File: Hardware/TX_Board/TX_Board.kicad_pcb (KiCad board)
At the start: 4 copper layers, 148 x 98.8 mm, 224 parts, among them IC1 GP2Y1+, IC10 QPA9122TR7, IC11 MAPS-010164-TR0500, IC12 QPA9122TR7, IC13 MAPS-010164-TR0500, IC14 QPA9122TR7, IC2 GP2Y1+, IC3 GP2Y1+, IC4 LT3041ADE#PBF, IC5 LT3099ADE#PBF, IC6 ADPL40502AUJZ-1.5-R7, IC7 MAPS-010164-TR0500, IC8 QPA9122TR7, IC9 MAPS-010164-TR0500, J1 Conn_Coaxial, J10 MM8030-2610RJ3, J11 MM8030-2610RJ3, J12 MM8030-2610RJ3, J13 MM8030-2610RJ3, J14 MM8030-2610RJ3, J15 Conn_Coaxial, J16 MM8030-2610RJ3, J17 MM8030-2610RJ3, J18 Conn_Coaxial, J19 MM8030-2610RJ3, J2 Conn_01x01_Pin, J20 MM8030-2610RJ3, J21 Conn_Coaxial, J22 MM8030-2610RJ3, J23 MM8030-2610RJ3, J24 Conn_Coaxial, J3 Conn_01x01_Pin, J4 Conn_01x01_Pin, J5 Conn_01x01_Pin, J6 Conn_02x12_Odd_Even, J7 Conn_01x03_Socket, J8 Conn_02x08_Odd_Even, J9 MM8030-2610RJ3, U1 SN74HCT138NSR

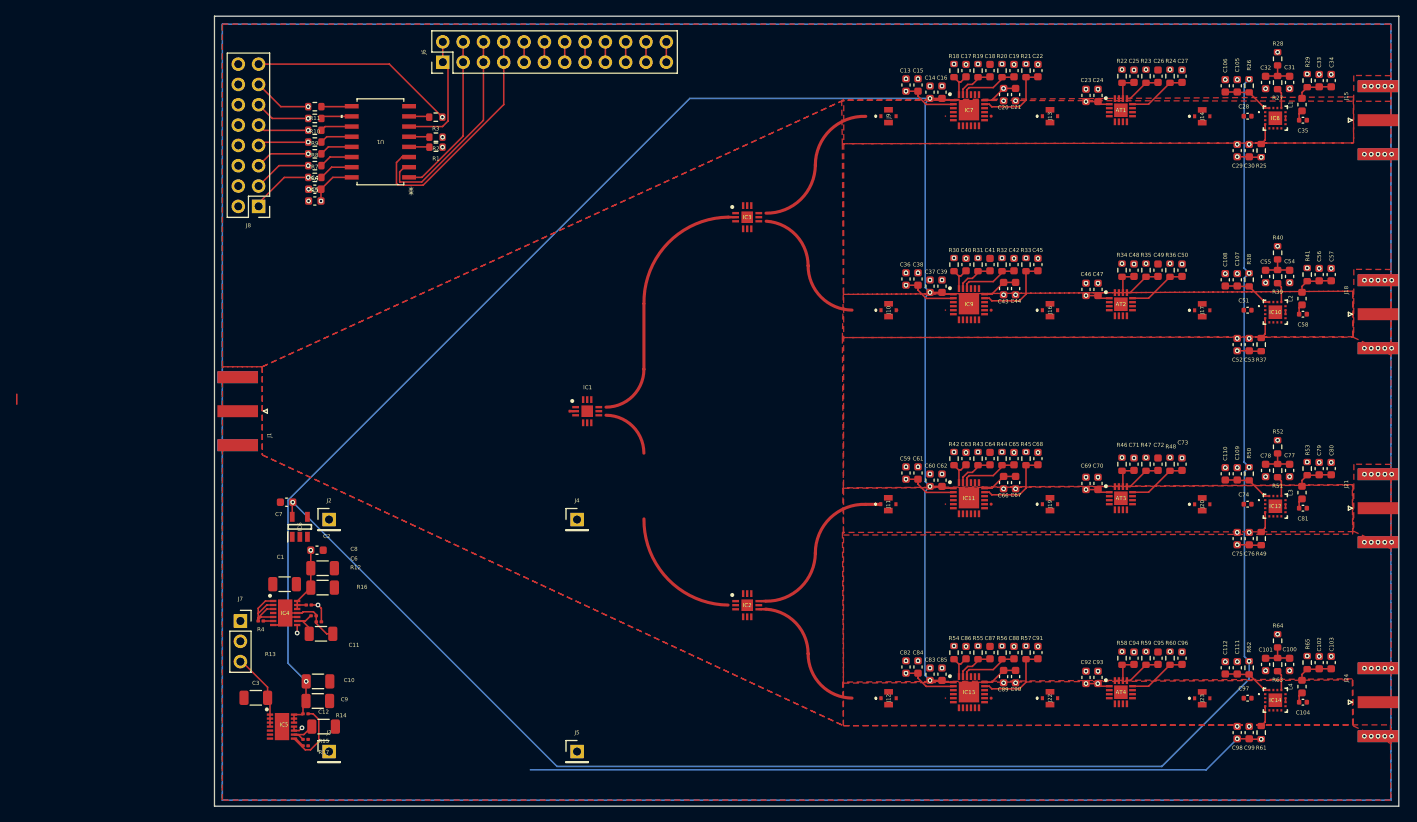
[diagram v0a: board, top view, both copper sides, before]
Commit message: Swapped layers
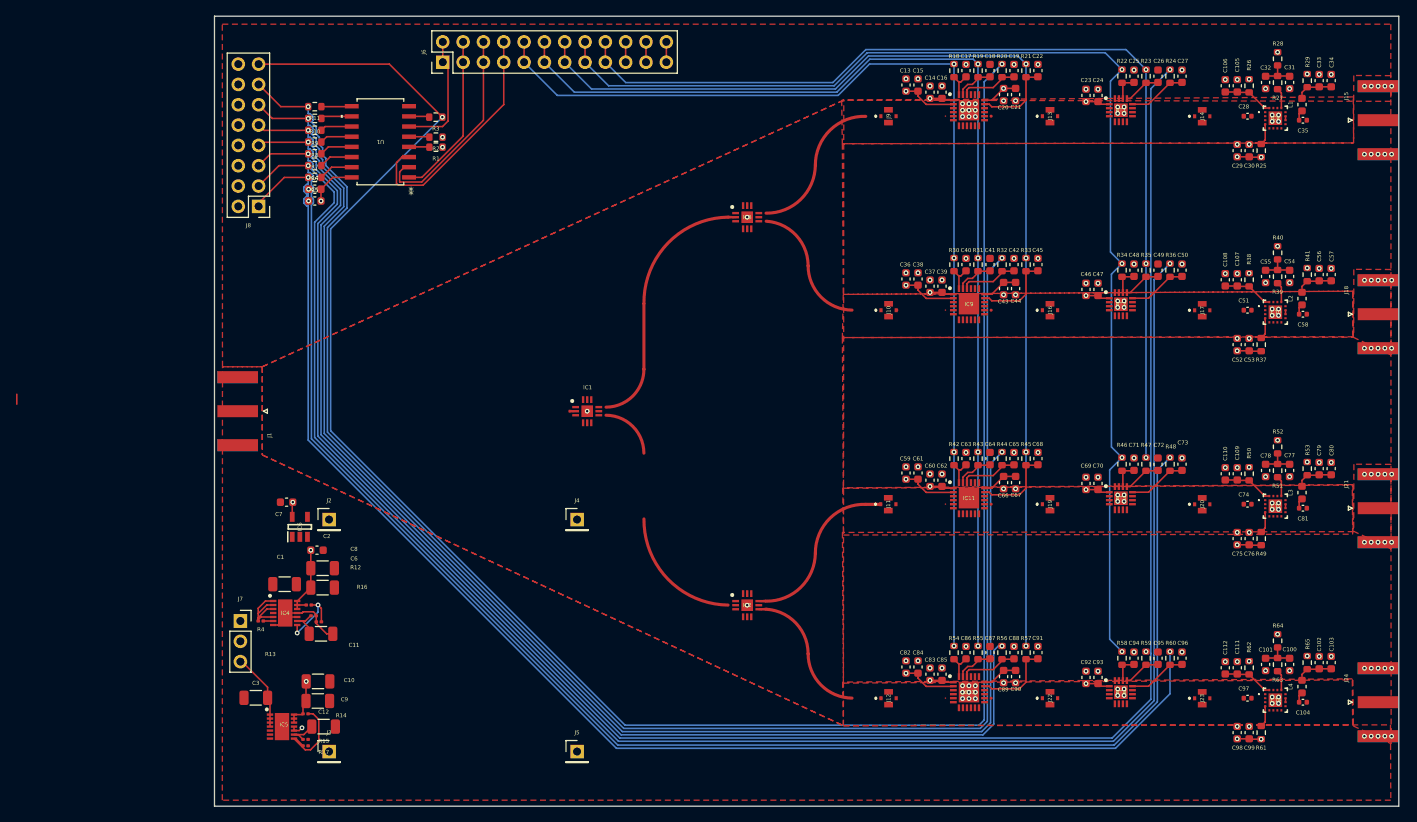
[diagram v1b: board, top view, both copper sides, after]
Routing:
- net PS_LE_3: track 177.7 -> 183.1 mm
- net PS_LE_2: track 202.9 -> 208.3 mm
- net PS_LE_1: track 245.5 -> 250.8 mm
- net PS_LE_4: track 154.6 -> 158.2 mm
- net ATTN_SI: track 146.2 -> 149.8 mm
- net ATTN_LE_2: track 219.8 -> 223.2 mm
- net ATTN_LE_1: track 244.1 -> 247.4 mm
- net ATTN_LE_3: track 194.2 -> 197.3 mm
- net VCC: vias 26 -> 25
- net GND: vias 129 -> 182
- added copper zone on In2.Cu, net VCC
- removed copper zone on B.Cu, net VCC

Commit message: Layout Tweaks
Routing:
- net VCC: track 175.2 -> 180.4 mm
- net VEE: track 217.3 -> 219.8 mm
- net GND: track 13.7 -> 11.8 mm, vias 182 -> 191
- net -VDC: track 9.57 -> 11.1 mm
- net Net-(IC5-PGFB): track 9.99 -> 11.3 mm
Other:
- board text added: "Phased and Confused Rev. 1 Rice ECE Capstone Team BEAMFORM"
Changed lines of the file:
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@@
 		(layer "Edge.Cuts")
 	)
+	(gr_text "Phased and Confused\nRev. 1\nRice ECE Capstone\nTeam BEAMFORM"
+		(at 84.529 68.072 0)
+		(layer "F.SilkS")
+		(effects
+			(font
+				(size 1.5 1.5)
+				(thickness 0.2)
+			)
+			(justify left bottom)
+		)
+	)
 	(gr_text "${REFERENCE}"
 		(at 183.195 49.88 270)
@@
 	)
 	(segment
-		(start 89.952 106.1)
-		(end 90.8 105.252)
+		(start 93.665 121.2)
+		(end 93.885 121.2)
 		(width 0.2)
 		(layer "F.Cu")
@@
 	)
 	(segment
-		(start 92.3 105.1)
-		(end 91.3 105.1)
+		(start 93.665 120.4)
+		(end 93.835 120.4)
 		(width 0.2)
 		(layer "F.Cu")
@@
 	)
 	(segment
-		(start 94.68 105.899999)
-		(end 95.980001 107.2)
+		(start 176.02 41.5)
+		(end 176.27 41.75)
+		(width 0.2)
+		(layer "F.Cu")
+		(net 1)
+	)
+	(segment
+		(start 92.3 105.1)
+		(end 91.3 105.1)
 		(width 0.2)
 		(layer "F.Cu")
@@
 	)
 	(segment
-		(start 91.3 105.1)
-		(end 90.8 104.6)
+		(start 94.68 105.899999)
+		(end 95.980001 107.2)
 		(width 0.2)
 		(layer "F.Cu")
@@
 	)
 	(segment
-		(start 94.67 104.79013)
-		(end 94.32887 104.449)
+		(start 93.885 121.2)
+		(end 94.26 120.825)
 		(width 0.2)
 		(layer "F.Cu")
@@
 	)
 	(segment
-		(start 92.3 104.6)
-		(end 90.8 104.6)
+		(start 94.67 104.79013)
+		(end 94.32887 104.449)
 		(width 0.2)
 		(layer "F.Cu")
@@
 	)
 	(segment
-		(start 90.8 105.252)
-		(end 90.8 104.6)
+		(start 94.32887 104.449)
+		(end 93.051 104.449)
 		(width 0.2)
 		(layer "F.Cu")
@@
 	)
 	(segment
-		(start 94.32887 104.449)
-		(end 93.051 104.449)
+		(start 93.835 120.4)
+		(end 94.26 120.825)
 		(width 0.2)
 		(layer "F.Cu")
@@
 	)
 	(segment
+		(start 176.02 42)
+		(end 176.27 41.75)
+		(width 0.2)
+		(layer "F.Cu")
+		(net 1)
+	)
+	(segment
 		(start 89.3 106.1)
 		(end 89.952 106.1)
@@
 	)
 	(via
+		(at 94.26 120.825)
+		(size 0.6)
+		(drill 0.3)
+		(layers "F.Cu" "B.Cu")
+		(free yes)
+		(net 1)
+	)
+	(via
 		(at 176.27 115.3)
 		(size 0.6)
@@
 	)
 	(via
+		(at 90.4 104.2)
+		(size 0.6)
+		(drill 0.3)
+		(layers "F.Cu" "B.Cu")
+		(net 1)
+	)
+	(via
 		(at 182.1 64.825)
 		(size 0.6)
@@
 	)
 	(via
+		(at 90.4 103.4)
+		(size 0.6)
+		(drill 0.3)
+		(layers "F.Cu" "B.Cu")
+		(net 1)
+	)
+	(via
 		(at 148.55 55.125)
 		(size 0.6)
@@
 	)
 	(via
+		(at 91.2 105.8)
+		(size 0.6)
+		(drill 0.3)
+		(layers "F.Cu" "B.Cu")
+		(net 1)
+	)
+	(via
 		(at 220.05 110.025)
 		(size 0.6)
@@
 	)
 	(via
+		(at 90.4 105)
+		(size 0.6)
+		(drill 0.3)
+		(layers "F.Cu" "B.Cu")
+		(net 1)
+	)
+	(via
 		(at 227.4 120)
 		(size 0.6)
@@
 	)
 	(via
+		(at 91.2 104.2)
+		(size 0.6)
+		(drill 0.3)
+		(layers "F.Cu" "B.Cu")
+		(net 1)
+	)
+	(via
 		(at 184.9 36.025)
 		(size 0.6)
@@
 	)
 	(via
+		(at 91.2 105)
+		(size 0.6)
+		(drill 0.3)
+		(layers "F.Cu" "B.Cu")
+		(net 1)
+	)
+	(via
 		(at 226.55 120)
 		(size 0.6)
@@
 	)
 	(via
+		(at 90.4 105.8)
+		(size 0.6)
+		(drill 0.3)
+		(layers "F.Cu" "B.Cu")
+		(net 1)
+	)
+	(via
 		(at 168.4 110.575)
 		(size 0.6)
@@
 	)
 	(via
+		(at 91.2 103.4)
+		(size 0.6)
+		(drill 0.3)
+		(layers "F.Cu" "B.Cu")
+		(net 1)
+	)
+	(via
 		(at 172.9 111.475)
 		(size 0.6)
@@
 	)
 	(segment
+		(start 94 95.5)
+		(end 93.58 95.08)
+		(width 0.2)
+		(layer "F.Cu")
+		(net 7)
+	)
+	(segment
 		(start 178.22 64.75)
 		(end 179.125 64.75)
@@
 	)
 	(segment
+		(start 94 96.75)
+		(end 92.773 96.75)
+		(width 0.2)
+		(layer "F.Cu")
+		(net 7)
+	)
+	(segment
 		(start 174.32 113.75)
 		(end 174.294 113.776)
@@
 	)
 	(segment
+		(start 91.68 95.657)
+		(end 91.68 95.08)
+		(width 0.2)
+		(layer "F.Cu")
+		(net 7)
+	)
+	(segment
 		(start 169.9 112.125)
 		(end 168.4 112.125)
@@
 	)
 	(segment
+		(start 92.773 96.75)
+		(end 91.68 95.657)
+		(width 0.2)
+		(layer "F.Cu")
+		(net 7)
+	)
+	(segment
 		(start 212.8 120.375)
 		(end 211.35 120.375)
@@
 	)
 	(segment
+		(start 94 96.75)
+		(end 94 95.5)
+		(width 0.2)
+		(layer "F.Cu")
+		(net 7)
+	)
+	(segment
 		(start 174.294 65.276)
 		(end 170.92589 65.276)
@@
 	)
 	(segment
+		(start 93.425 113.15)
+		(end 88.171 107.896)
+		(width 0.2)
+		(layer "In2.Cu")
+		(net 21)
+	)
+	(segment
 		(start 141.375057 40.275)
 		(end 171.4 40.275)
@@
 	)
 	(segment
-		(start 91.149 110.874)
-		(end 91.149 90.501057)
+		(start 170.799 88.174)
+		(end 170.799 65.126)
 		(width 0.2)
 		(layer "In2.Cu")
@@
 	)
 	(segment
-		(start 170.799 88.174)
-		(end 170.799 65.126)
+		(start 88.171 107.896)
+		(end 88.171 93.479057)
 		(width 0.2)
 		(layer "In2.Cu")
@@
 	)
 	(segment
-		(start 93.425 113.15)
-		(end 91.149 110.874)
-		(width 0.2)
-		(layer "In2.Cu")
-		(net 21)
-	)
-	(segment
 		(start 170.77 112.395)
 		(end 170.77 89.405)
@@
 	)
 	(segment
-		(start 91.149 90.501057)
-		(end 141.375057 40.275)
+		(start 170.799 40.876)
+		(end 171.4 40.275)
 		(width 0.2)
 		(layer "In2.Cu")
@@
 	)
 	(segment
-		(start 170.799 40.876)
-		(end 171.4 40.275)
+		(start 88.171 93.479057)
+		(end 141.375057 40.275)
 		(width 0.2)
 		(layer "In2.Cu")
@@
 	)
 	(segment
-		(start 95.001 120.66387)
+		(start 95.001 121.567)
 		(end 95.001 117.91484)
 		(width 0.2)
@@
 	(segment
 		(start 91.9 120.3)
-		(end 93.301 121.701)
+		(end 91.9 121.071)
 		(width 0.2)
 		(layer "F.Cu")
@@
 	)
 	(segment
-		(start 94.28616 117.2)
-		(end 93.665 117.2)
+		(start 91.9 120.3)
+		(end 92.125 120.3)
 		(width 0.2)
 		(layer "F.Cu")
@@
 	)
 	(segment
-		(start 91.9 120.3)
-		(end 92.125 120.3)
+		(start 95.001 117.91484)
+		(end 94.28616 117.2)
 		(width 0.2)
 		(layer "F.Cu")
@@
 	)
 	(segment
-		(start 93.96387 121.701)
-		(end 95.001 120.66387)
+		(start 94.28616 117.2)
+		(end 93.665 117.2)
 		(width 0.2)
 		(layer "F.Cu")
@@
 	)
 	(segment
-		(start 93.301 121.701)
-		(end 93.96387 121.701)
+		(start 92.984 122.155)
+		(end 94.413 122.155)
 		(width 0.2)
 		(layer "F.Cu")
@@
 	)
 	(segment
-		(start 95.001 117.91484)
-		(end 94.28616 117.2)
+		(start 92.125 120.3)
+		(end 93.025 121.2)
 		(width 0.2)
 		(layer "F.Cu")
@@
 	)
 	(segment
-		(start 92.125 120.3)
-		(end 93.025 121.2)
+		(start 91.9 121.071)
+		(end 92.984 122.155)
+		(width 0.2)
+		(layer "F.Cu")
+		(net 46)
+	)
+	(segment
+		(start 94.413 122.155)
+		(end 95.001 121.567)
 		(width 0.2)
 		(layer "F.Cu")
@@
 	)
 	(segment
+		(start 90.4 118.8)
+		(end 88.9 118.8)
+		(width 0.2)
+		(layer "F.Cu")
+		(net 55)
+	)
+	(segment
 		(start 88.9 117.3)
 		(end 88.9 117.8)
@@
 		(polygon
 			(pts
-				(xy 87.93 73.82) (xy 82.96 73.82) (xy 82.94 31) (xy 229 31) (xy 229 40.64) (xy 160.62 40.49)
+				(xy 87.93 73.82) (xy 82.96 73.82) (xy 82.94 31) (xy 229 31) (xy 229 41.538503) (xy 158.795 41.633)
 			)
 		)
@@
 		(polygon
 			(pts
-				(xy 160.360026 40.491633) (xy 160.440008 45.940408) (xy 224.35 45.84) (xy 224.31 40.09)
+				(xy 160.375713 41.560231) (xy 160.440008 45.940408) (xy 224.35 45.84) (xy 224.317435 41.15865)
 			)
 		)

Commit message: DRC and more layout
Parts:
- R4: footprint Resistor_SMD:R_0201_0603Metric -> Resistor_SMD:R_0603_1608Metric
- moved R4 0.30 mm to (87.7, 105.3), turned to 90 degrees
- moved R2 0.28 mm to (109.6, 44.8)
- moved C92 0.09 mm to (190.9, 112.6)
- moved C93 0.09 mm to (192.4, 112.6)
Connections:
- AT1 pad 15: ATTN_A1 -> GND
- AT1 pad 16: ATTN_A2 -> GND
- AT1 pad 2: ATTN_A0 -> GND
- AT2 pad 15: ATTN_A1 -> GND
- AT2 pad 16: ATTN_A2 -> GND
- AT2 pad 2: ATTN_A0 -> GND
- AT3 pad 15: ATTN_A1 -> GND
- AT3 pad 16: ATTN_A2 -> GND
- AT3 pad 2: ATTN_A0 -> GND
- AT4 pad 15: ATTN_A1 -> GND
- AT4 pad 16: ATTN_A2 -> GND
- AT4 pad 2: ATTN_A0 -> GND
- J6 pad 19: ATTN_A0 -> GND
- J6 pad 20: ATTN_A0 -> GND
- J6 pad 21: ATTN_A1 -> GND
- J6 pad 22: ATTN_A1 -> GND
- J6 pad 23: ATTN_A2 -> GND
- J6 pad 24: ATTN_A2 -> GND
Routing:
- net GND: track 11.8 -> 175.3 mm, vias 191 -> 344
- net VCC: track 180.4 -> 231.5 mm, vias 25 -> 46
- net ATTN_CLK: track 122.4 -> 146.7 mm, vias 4 -> 7
- net VEE: track 219.8 -> 230.6 mm, vias 5 -> 8
- net Net-(IC13-SER_OUT): track 10.1 -> 20.1 mm
- net Net-(IC11-SER_OUT): track 10.1 -> 20.1 mm
- net Net-(IC9-SER_OUT): track 10.1 -> 20.1 mm
- net /TX_Channel3/AMP-RF_OUT: track 8.90 -> 17.8 mm
- net /TX_Channel2/AMP-RF_OUT: track 8.90 -> 17.8 mm
- net /TX_Channel1/AMP-RF_OUT: track 8.90 -> 17.8 mm
- net Net-(AT2-LE): track 7.32 -> 14.6 mm
- net Net-(AT3-LE): track 7.32 -> 14.6 mm
- net Net-(AT4-LE): track 7.32 -> 14.6 mm
- net Net-(IC9-D3_OR_LE): track 7.15 -> 14.3 mm
- net Net-(IC11-D3_OR_LE): track 7.15 -> 14.3 mm
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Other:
- board size 148 x 98.8 mm -> 148.3 x 98.8 mm
- board text removed: "${REFERENCE}"

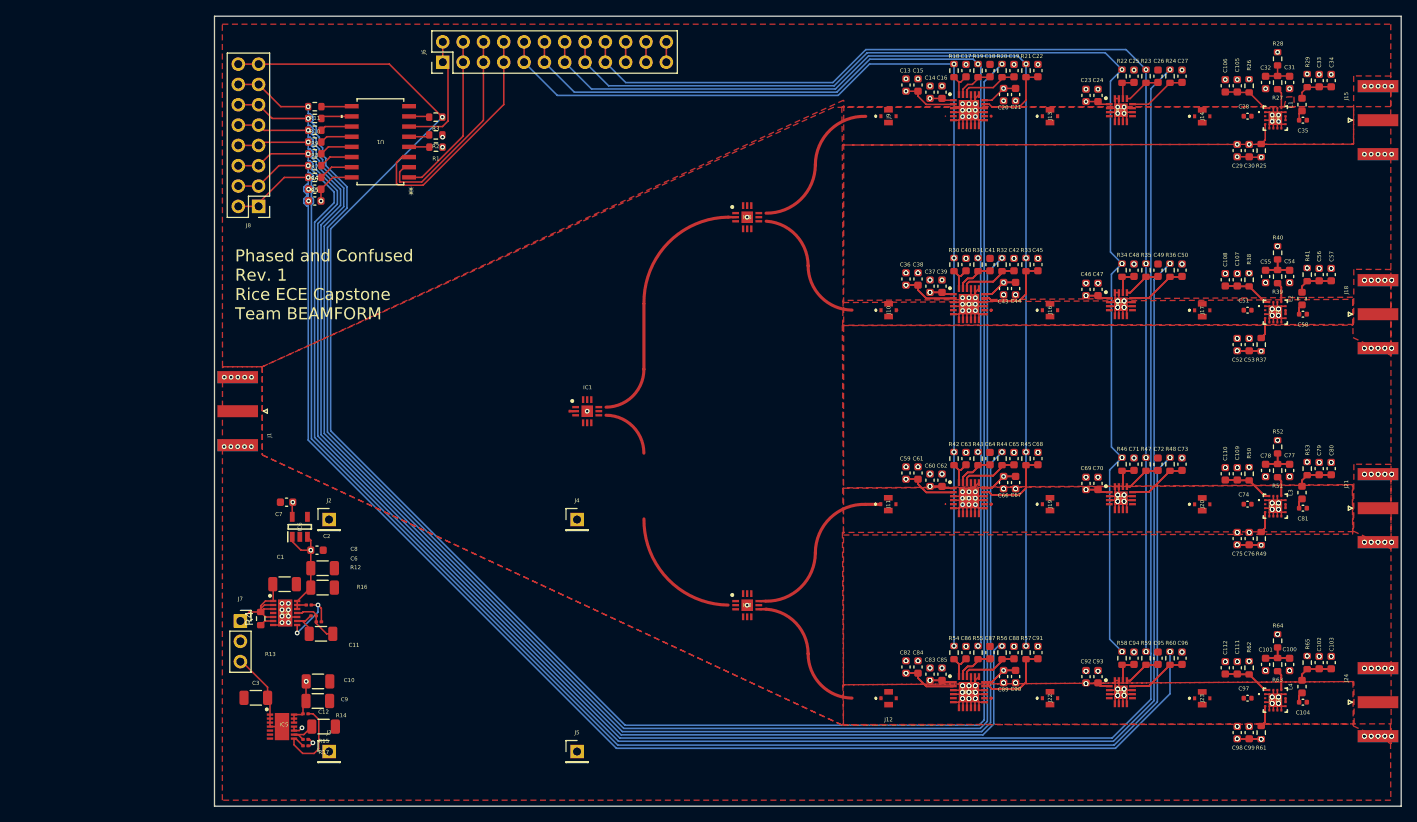
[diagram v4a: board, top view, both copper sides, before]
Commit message: removed via in pad
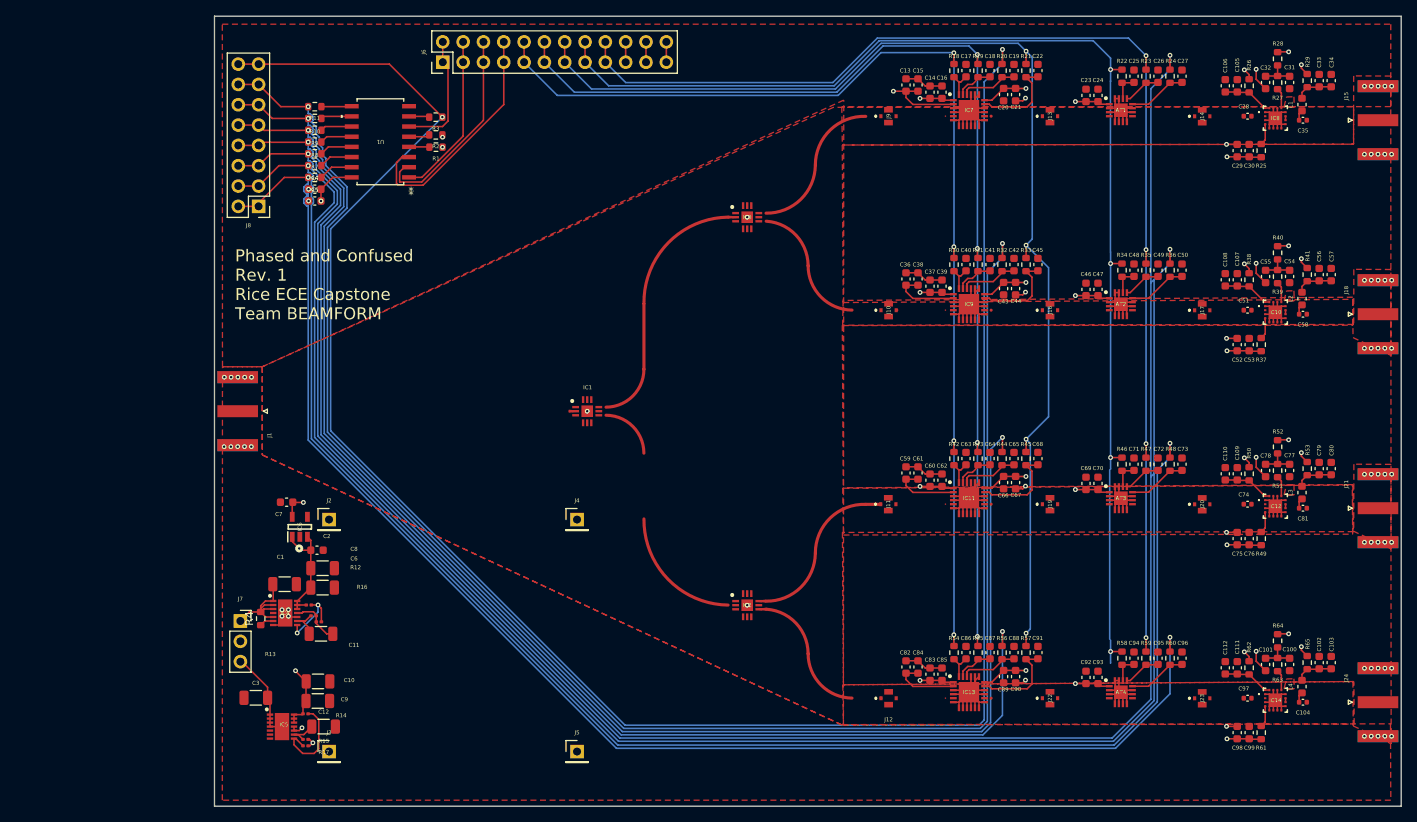
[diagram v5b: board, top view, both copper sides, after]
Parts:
- moved C92 0.09 mm to (190.9, 112.7)
- moved C93 0.09 mm to (192.4, 112.7)
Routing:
- net VCC: track 231.5 -> 125.5 mm, vias 46 -> 23
- net GND: track 175.3 -> 219.5 mm, vias 344 -> 75
- net PS_SER_OUT: track 136.5 -> 147.0 mm, vias 7 -> 4
- net /TX_Channel3/AMP-RF_OUT: track 17.8 -> 8.90 mm
- net /TX_Channel2/AMP-RF_OUT: track 17.8 -> 8.90 mm
- net /TX_Channel1/AMP-RF_OUT: track 17.8 -> 8.90 mm
- net Net-(IC13-SER_OUT): track 20.1 -> 11.2 mm
- net Net-(IC11-SER_OUT): track 20.1 -> 11.2 mm
- net Net-(IC9-SER_OUT): track 20.1 -> 11.2 mm
- net PS_SER_IN: track 132.4 -> 140.2 mm, vias 7 -> 4
- net ATTN_CLK: track 146.7 -> 154.1 mm, vias 7 -> 4
- net Net-(AT2-LE): track 14.6 -> 7.32 mm
- net Net-(AT3-LE): track 14.6 -> 7.32 mm
- net Net-(AT4-LE): track 14.6 -> 7.32 mm
- net Net-(IC9-D3_OR_LE): track 14.3 -> 7.15 mm
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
